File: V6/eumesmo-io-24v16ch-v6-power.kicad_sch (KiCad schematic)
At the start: 50 parts, among them J6 250-202, J7 USB_C_Receptacle_USB2.0, Q1 WPM2015-3/TR, Q2 MMUN2211LT3G, U1 TX4138, U2 SY8089A1AAC

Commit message: Replaced white leds for emerald.
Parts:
- D6: value WHITE/0603 -> EMERALD/0603; LCSC Part # C2290 -> C2984266; Mfr Hubei KENTO Elec -> Everlight Elec; Mfr PN KT-0603W -> 19-213/GHC-XS1T1N/5T; Technology (none) -> LED; Vendor PN C2290 -> C2984266
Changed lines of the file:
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@@
 			)
 		)
-		(property "Value" "WHITE/0603"
+		(property "Value" "EMERALD/0603"
 			(at 124.46 152.4 90)
 			(show_name no)
@@
 			)
 		)
-		(property "Mfr" "Hubei KENTO Elec"
+		(property "Mfr" "Everlight Elec"
 			(at 121.92 152.4 0)
 			(hide yes)
@@
 			)
 		)
-		(property "Mfr PN" "KT-0603W"
+		(property "Mfr PN" "19-213/GHC-XS1T1N/5T"
 			(at 121.92 152.4 0)
 			(hide yes)
@@
 			)
 		)
-		(property "Technology" ""
+		(property "Technology" "LED"
 			(at 121.92 152.4 0)
 			(hide yes)
@@
 			)
 		)
-		(property "Vendor PN" "C2290"
+		(property "Vendor PN" "C2984266"
 			(at 121.92 152.4 0)
 			(hide yes)
@@
 			)
 		)
-		(property "LCSC Part #" "C2290"
+		(property "LCSC Part #" "C2984266"
 			(at 124.46 154.94 90)
 			(show_name no)

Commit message: Remove jumpers from BOM.
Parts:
- C1, C2, D6: FT Rotation Offset 0 -> 180
- D5: FT Rotation Offset -90 -> 90
- J7: FT Rotation Offset 180 -> 0
- JP2, TP2, TP3, TP7: now not fitted; now left out of the parts list
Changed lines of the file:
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@@
 		(body_style 1)
 		(exclude_from_sim no)
-		(in_bom yes)
+		(in_bom no)
 		(on_board yes)
 		(in_pos_files yes)
-		(dnp no)
+		(dnp yes)
 		(fields_autoplaced yes)
 		(property "Reference" "JP2"
@@
 			)
 		)
-		(property "FT Rotation Offset" "-90"
+		(property "FT Rotation Offset" "90"
 			(at 105.41 100.33 0)
 			(hide yes)
@@
 		(body_style 1)
 		(exclude_from_sim no)
-		(in_bom yes)
+		(in_bom no)
 		(on_board yes)
 		(in_pos_files yes)
-		(dnp no)
+		(dnp yes)
 		(property "Reference" "TP7"
 			(at 111.76 121.92 0)
@@
 			)
 		)
-		(property "FT Rotation Offset" "0"
+		(property "FT Rotation Offset" "180"
 			(at 121.92 152.4 90)
 			(hide yes)
@@
 			)
 		)
-		(property "FT Rotation Offset" "0"
+		(property "FT Rotation Offset" "180"
 			(at 168.91 34.29 0)
 			(hide yes)
@@
 		(body_style 1)
 		(exclude_from_sim no)
-		(in_bom yes)
+		(in_bom no)
 		(on_board yes)
 		(in_pos_files yes)
-		(dnp no)
+		(dnp yes)
 		(property "Reference" "TP2"
 			(at 266.7 29.21 0)
@@
 		(body_style 1)
 		(exclude_from_sim no)
-		(in_bom yes)
+		(in_bom no)
 		(on_board yes)
 		(in_pos_files yes)
-		(dnp no)
+		(dnp yes)
 		(property "Reference" "TP3"
 			(at 50.8 36.83 0)
@@
 			)
 		)
-		(property "FT Rotation Offset" "0"
+		(property "FT Rotation Offset" "180"
 			(at 69.85 35.56 0)
 			(hide yes)
@@
 			)
 		)
-		(property "FT Rotation Offset" "180"
+		(property "FT Rotation Offset" "0"
 			(at 43.18 85.09 0)
 			(hide yes)

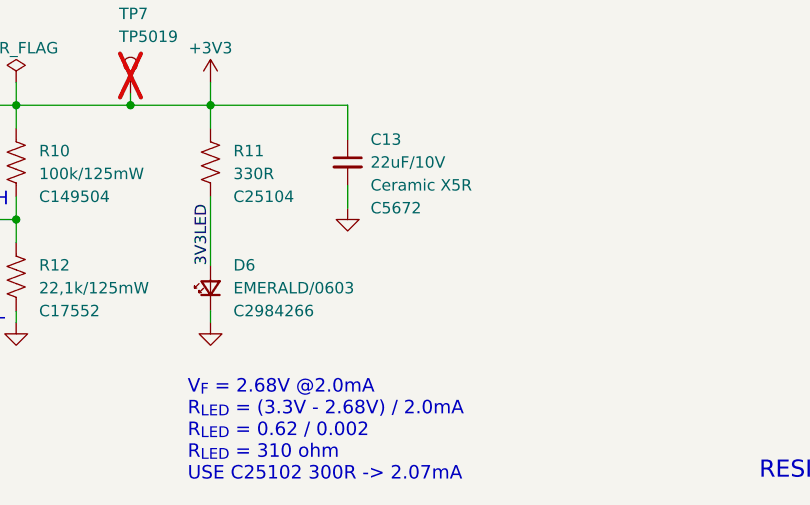
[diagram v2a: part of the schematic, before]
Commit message: LEDs changed to orange
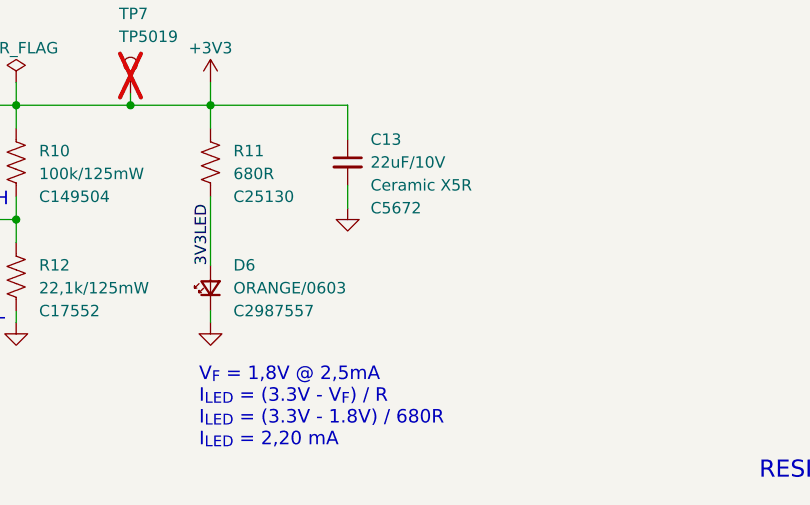
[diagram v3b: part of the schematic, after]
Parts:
- D6: value EMERALD/0603 -> ORANGE/0603; FT Rotation Offset 180 -> 0; LCSC Part # C2984266 -> C2987557; Mfr PN 19-213/GHC-XS1T1N/5T -> 19-217/S2C-AL1M2VY/6T; Vendor PN C2984266 -> C2987557
- R11: value 330R -> 680R; LCSC Part # C25104 -> C25130; Mfr PN 0402WGF3300TCE -> 0402WGF6800TCE; Vendor PN C25104 -> C25130
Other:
- note added: "V_{F} = 1,8V @ 2,5mA I_{LED} = (3.3V - V_{F}) / R I_{LED} = (3.3V - 1.8V) / 680R I_{LED} = 2,20 mA"
- note removed: "V_{F} = 2.68V @2.0mA R_{LED} = (3.3V - 2.68V) / 2.0mA R_{LED} = 0.62 / 0.002 R_{LED} = 310 ohm USE C25102 300R -> 2.07mA"
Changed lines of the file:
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@@
 		)
 	)
-	(text "V_{F} = 2.68V @2.0mA\nR_{LED} = (3.3V - 2.68V) / 2.0mA\nR_{LED} = 0.62 / 0.002\nR_{LED} = 310 ohm\nUSE C25102 300R -> 2.07mA"
-		(exclude_from_sim no)
-		(at 119.38 173.99 0)
-		(effects
-			(font
-				(size 1.5 1.5)
-			)
-			(justify left bottom)
-		)
-	)
 	(text "R_{H} = (V_{OUT} - 0,6V) * R_{L} / 0,6V\n\nV_{OUT} = (0,6 * R_{H} / R_{L}) + 0,6\nV_{OUT} = (0,6 * 100k/22,1k) +0,6\nV_{OUT} = 3,31V"
 		(exclude_from_sim no)
@@
 		)
 	)
+	(text "V_{F} = 1,8V @ 2,5mA\nI_{LED} = (3.3V - V_{F}) / R\nI_{LED} = (3.3V - 1.8V) / 680R\nI_{LED} = 2,20 mA"
+		(exclude_from_sim no)
+		(at 120.65 170.18 0)
+		(effects
+			(font
+				(size 1.5 1.5)
+			)
+			(justify left bottom)
+		)
+	)
 	(text "24VDC"
 		(exclude_from_sim no)
@@
 			)
 		)
-		(property "Value" "330R"
+		(property "Value" "680R"
 			(at 124.46 139.7 0)
 			(show_name no)
@@
 			)
 		)
-		(property "Mfr PN" "0402WGF3300TCE"
+		(property "Mfr PN" "0402WGF6800TCE"
 			(at 121.92 138.43 0)
 			(hide yes)
@@
 			)
 		)
-		(property "Vendor PN" "C25104"
+		(property "Vendor PN" "C25130"
 			(at 121.92 138.43 0)
 			(hide yes)
@@
 			)
 		)
-		(property "LCSC Part #" "C25104"
+		(property "LCSC Part #" "C25130"
 			(at 124.46 142.24 0)
 			(show_name no)
@@
 			)
 		)
-		(property "Value" "EMERALD/0603"
+		(property "Value" "ORANGE/0603"
 			(at 124.46 152.4 90)
 			(show_name no)
@@
 			)
 		)
-		(property "Mfr PN" "19-213/GHC-XS1T1N/5T"
+		(property "Mfr PN" "19-217/S2C-AL1M2VY/6T"
 			(at 121.92 152.4 0)
 			(hide yes)
@@
 			)
 		)
-		(property "Vendor PN" "C2984266"
+		(property "Vendor PN" "C2987557"
 			(at 121.92 152.4 0)
 			(hide yes)
@@
 			)
 		)
-		(property "LCSC Part #" "C2984266"
+		(property "LCSC Part #" "C2987557"
 			(at 124.46 154.94 90)
 			(show_name no)
@@
 			)
 		)
-		(property "FT Rotation Offset" "180"
+		(property "FT Rotation Offset" "0"
 			(at 121.92 152.4 90)
 			(hide yes)

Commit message: Adjusted component rotation and offset information for JLCPCB.
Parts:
- C1: FT Rotation Offset 180 -> 0
- C5: FT Rotation Offset 0 -> 180

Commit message: Replaced Wago connectors for other brand, no stock.
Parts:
- J6: LCSC Part # C2765061 -> C475154; Mfr Wago -> Cixi Kefa Elec; Mfr PN 250-202 -> KF250-3.5-2P-1; Vendor PN C2765061 -> C475154
- R11: LCSC Part # C25130 -> C137948; Mfr Uniroyal -> YAGEO; Mfr PN 0402WGF6800TCE -> RC0402FR-07680RL; Vendor PN C25130 -> C137948
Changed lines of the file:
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@@
 			)
 		)
-		(property "Mfr" "Uniroyal"
+		(property "Mfr" "YAGEO"
 			(at 121.92 138.43 0)
 			(hide yes)
@@
 			)
 		)
-		(property "Mfr PN" "0402WGF6800TCE"
+		(property "Mfr PN" "RC0402FR-07680RL"
 			(at 121.92 138.43 0)
 			(hide yes)
@@
 			)
 		)
-		(property "Vendor PN" "C25130"
+		(property "Vendor PN" "C137948"
 			(at 121.92 138.43 0)
 			(hide yes)
@@
 			)
 		)
-		(property "LCSC Part #" "C25130"
+		(property "LCSC Part #" "C137948"
 			(at 124.46 142.24 0)
 			(show_name no)
@@
 			)
 		)
-		(property "Mfr" "Wago"
+		(property "Mfr" "Cixi Kefa Elec"
 			(at 34.29 29.21 0)
 			(hide yes)
@@
 			)
 		)
-		(property "Mfr PN" "250-202"
+		(property "Mfr PN" "KF250-3.5-2P-1"
 			(at 34.29 29.21 0)
 			(hide yes)
@@
 			)
 		)
-		(property "Vendor PN" "C2765061"
+		(property "Vendor PN" "C475154"
 			(at 34.29 29.21 0)
 			(hide yes)
@@
 			)
 		)
-		(property "LCSC Part #" "C2765061"
+		(property "LCSC Part #" "C475154"
 			(at 34.29 29.21 0)
 			(hide yes)
